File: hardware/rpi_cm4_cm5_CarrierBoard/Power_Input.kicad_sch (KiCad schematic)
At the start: 19 parts, among them Q9 IPD60R360P7ATMA1, U23 LTC4359IDCB

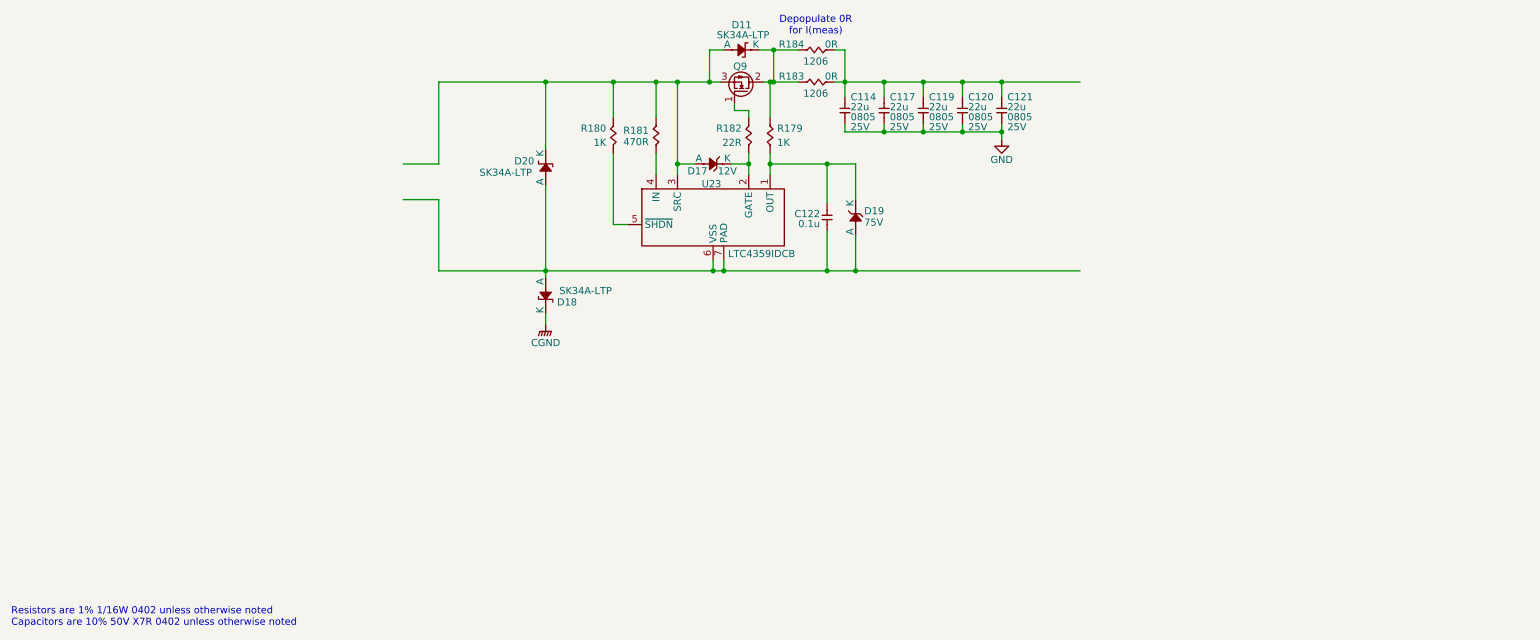
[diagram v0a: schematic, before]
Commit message: Significant update to schematics Add codec, Mikrobus, PIC32A Add power table, design notes for pinmux Add datasheets
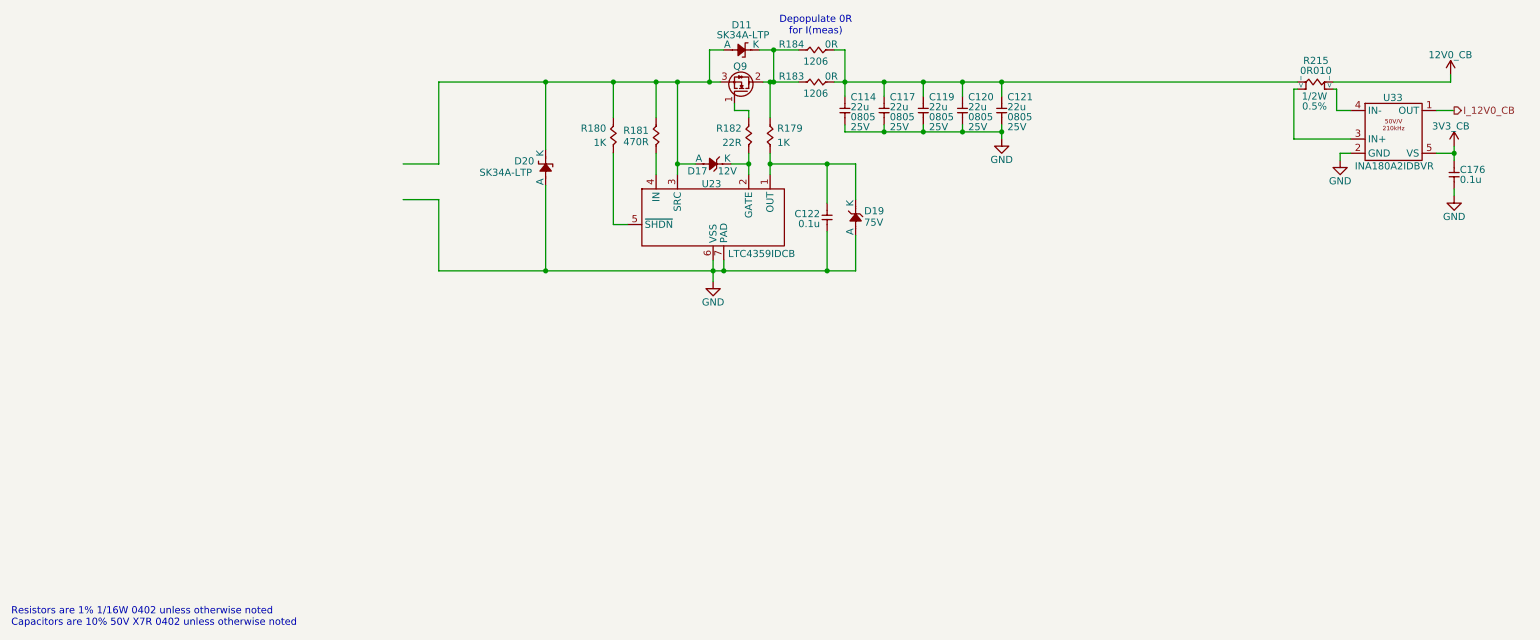
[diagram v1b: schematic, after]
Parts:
- removed D18: SK34A-LTP, footprint:DO-214AC, symbol KicadCompDb:Diodes/DIODE_00005
- added C176: 0.1u, footprint:CAP_NONPOL_0402, symbol KicadCompDb:Capacitors/CAP_CER_SMT_00001
- added R215: 0R010, footprint:RES_SENSE_1206, symbol KicadCompDb:Resistors/RES_SMT_00033
- added U33: INA180A2IDBVR, footprint:SOT-23-5, symbol KicadCompDb:Amplifier/AMP_00001
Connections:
- net GND: now also C122.1, D19.2 (A), D20.2 (A), U23.6 (VSS), U23.7 (PAD), C176.1, U33.2 (GND)
- net at C114.2, C117.2, C119.2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: now also R215.1 (I)
- new net: R215.2 (V), U33.3 (IN+)
- new net: R215.3 (V), U33.4 (IN-)
- new net 12V0_CB: R215.4 (I)
- new net 3V3_CB: C176.2, U33.5 (VS)
- new net I_12V0_CB: U33.1 (OUT)
